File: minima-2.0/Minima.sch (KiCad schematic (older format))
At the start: 11 parts

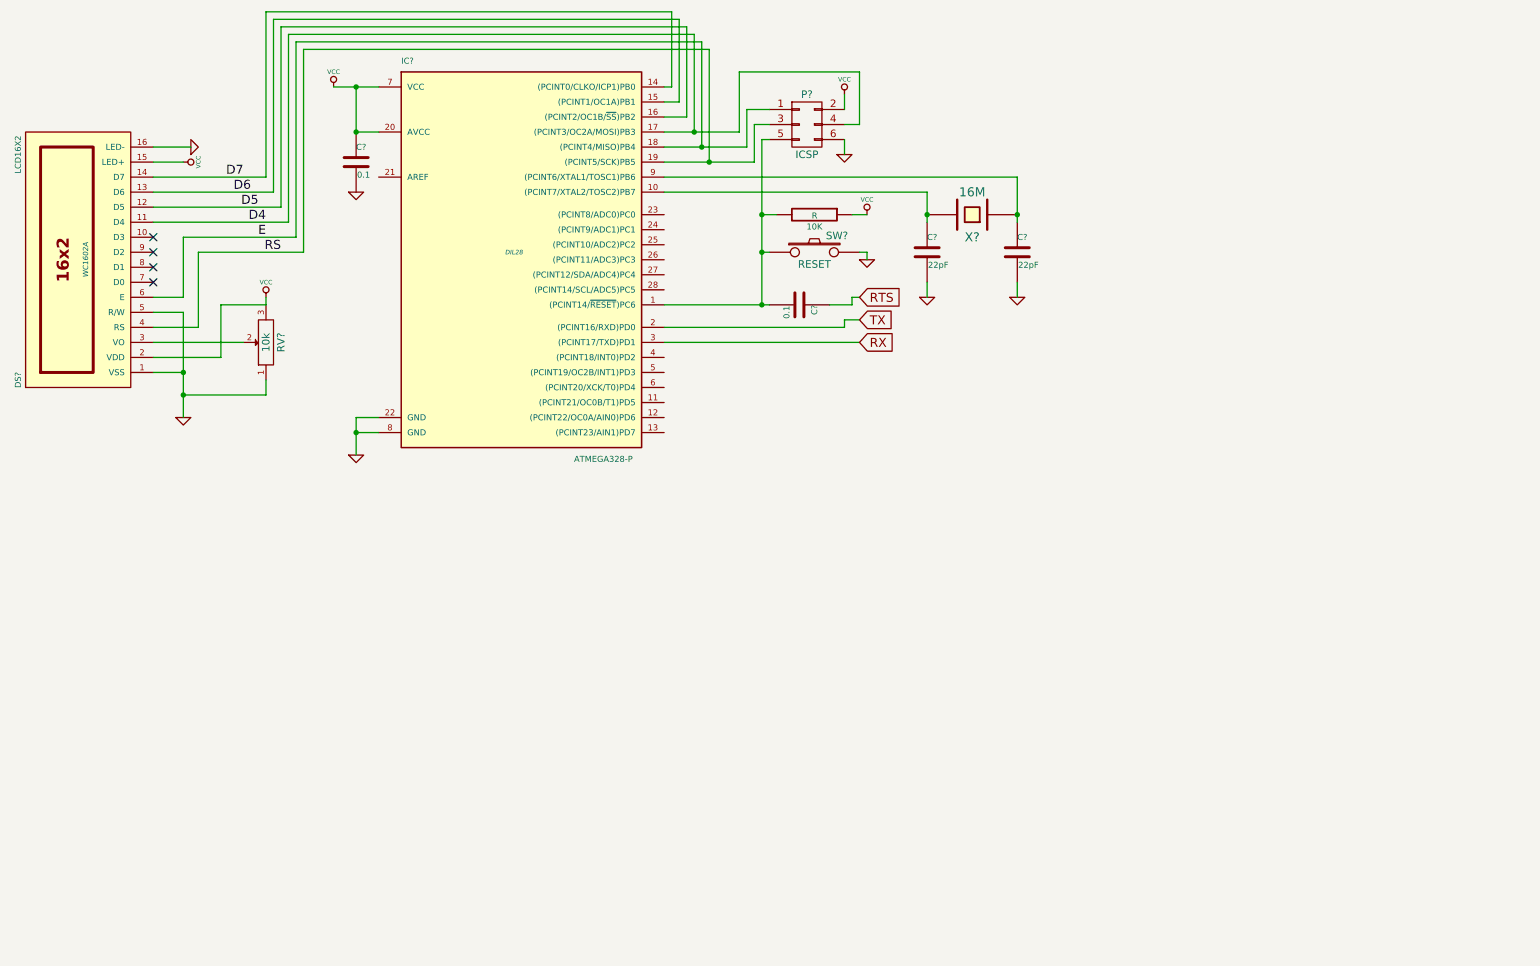
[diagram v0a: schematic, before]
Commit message: Finalized a first version of the front panel board
 - Added the Si570 on the front panel board
 - Split TX/RX and PTT
 - Inverted PD3 and PD4 for potential tone generator
 - Added multiple buttons via analog multiplexing
 - Added rotary encoder
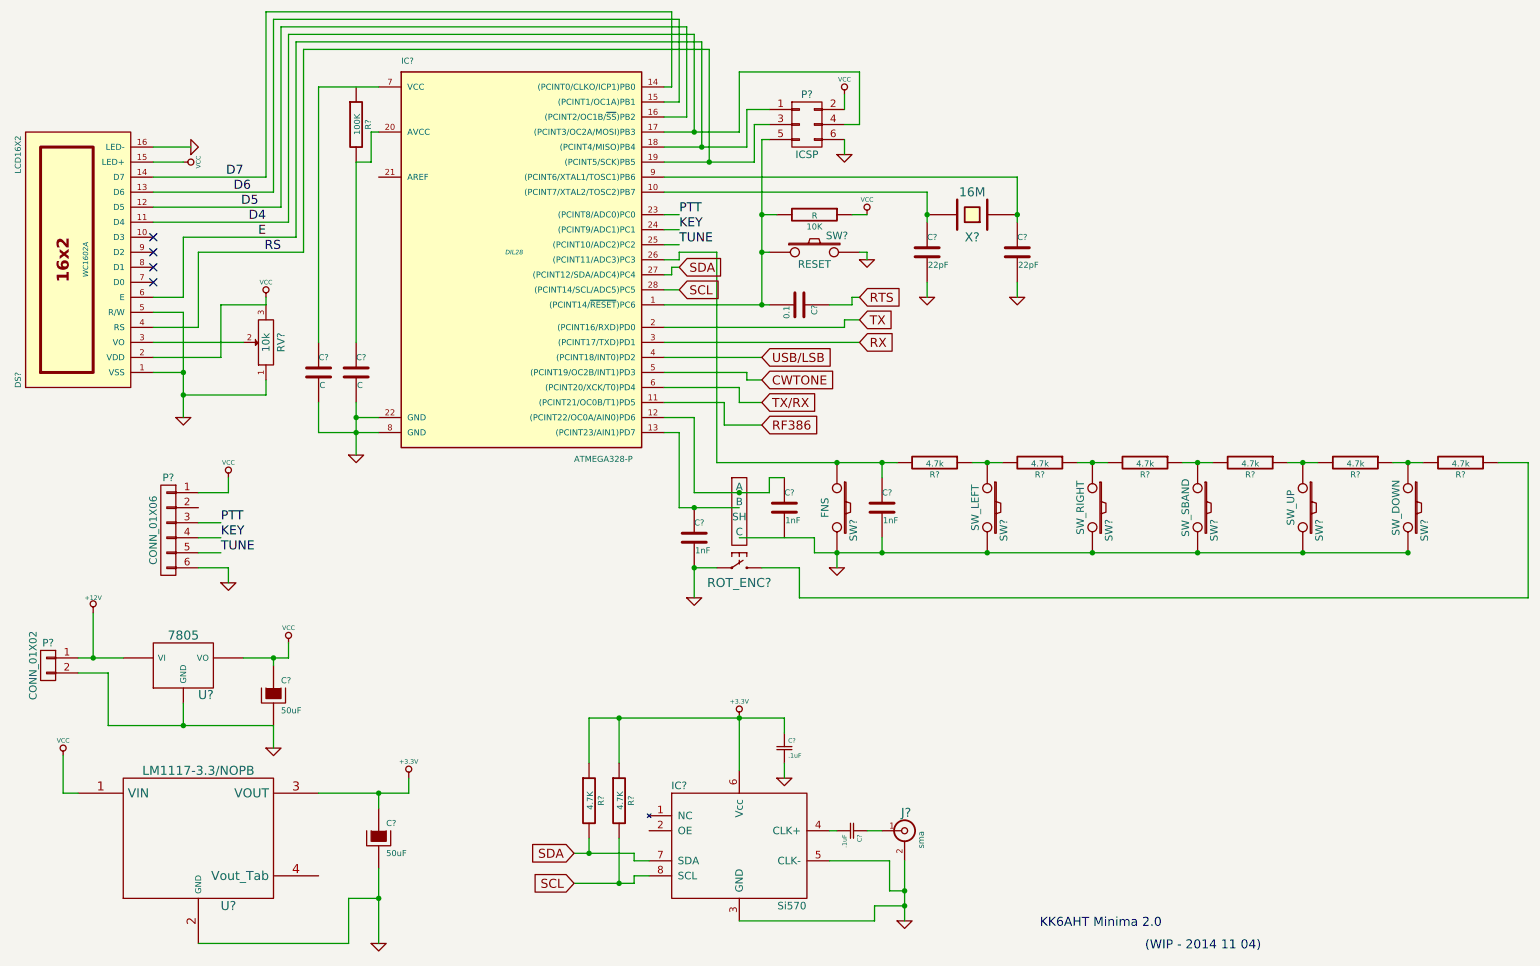
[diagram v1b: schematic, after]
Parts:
- removed C?: 0.1, symbol C
- added C? (x3): 1nF, symbol C
- added C? (x2): 50uF, symbol CP
- added C? (x2): .1uF, symbol Csmall
- added C? (x2): C, symbol C
- added IC?: Si570, SI570_SI571_Standard, symbol Si570
- added J?: sma, sma, symbol sma
- added P?: CONN_01X06, symbol CONN_01X06
- added P?: CONN_01X02, symbol CONN_01X02
- added R? (x6): 4.7k, symbol R
- added R? (x2): 4.7K, symbol R
- added R?: 100K, symbol R
- added ROT_ENC?: AB2_ROTARY_ENCODER_W_SW, symbol AB2_ROTARY_ENCODER_W_SW
- added SW?: FNS, symbol SW_PUSH
- added SW?: SW_LEFT, symbol SW_PUSH
- added SW?: SW_RIGHT, symbol SW_PUSH
- added SW?: SW_SBAND, symbol SW_PUSH
- added SW?: SW_UP, symbol SW_PUSH
- added SW?: SW_DOWN, symbol SW_PUSH
- added U?: LM1117-3.3/NOPB, SOT223, symbol LM1117-3.3/NOPB
- added U?: 7805, symbol 7805
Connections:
- net GND: now also C?.2, C?.2, C?.2, C?.2, C?.2, C?.2, C?.2, IC?.3 (GND), IC?.5 (CLK-), J?.2 (Ext), P?.2 (P2), P?.6 (P6), ROT_ENC?.2 (C), ROT_ENC?.4, SW?.2, SW?.2, SW?.2, SW?.2, SW?.2, SW?.2, U?.2 (GND), U?.GND
- net VCC: now also C?.1, P?.1 (P1), U?.1 (VIN), U?.VO; no longer IC?.20 (AVCC), IC?.7 (VCC)
- net RF386: now reaches IC?.11 ((PCINT21/OC0B/T1)PD5)
- net at IC?.12 ((PCINT22/OC0A/AIN0)PD6): now also C?.1, ROT_ENC?.1 (A)
- net at IC?.13 ((PCINT23/AIN1)PD7): now also C?.1, ROT_ENC?.3 (B)
- net PTT: now reaches IC?.23 ((PCINT8/ADC0)PC0)
- net PTT: now also P?.3 (P3)
- net KEY: now reaches IC?.24 ((PCINT9/ADC1)PC1)
- net KEY: now also P?.4 (P4)
- net TUNE: now reaches IC?.25 ((PCINT10/ADC2)PC2)
- net TUNE: now also P?.5 (P5)
- net at IC?.26 ((PCINT11/ADC3)PC3): now also C?.1, R?.2, SW?.1
- net SDA: now reaches IC?.27 ((PCINT12/SDA/ADC4)PC4)
- net SDA: now also IC?.7 (SDA), R?.2
- net SCL: now reaches IC?.28 ((PCINT14/SCL/ADC5)PC5)
- net SCL: now also IC?.8 (SCL), R?.2
- net USB/LSB: now reaches IC?.4 ((PCINT18/INT0)PD2)
- net CWTONE: now reaches IC?.5 ((PCINT19/OC2B/INT1)PD3)
- net TX/RX: now reaches IC?.6 ((PCINT20/XCK/T0)PD4)
- new net: C?.1, IC?.20 (AVCC), R?.2
- new net: C?.1, IC?.7 (VCC)
- new net: R?.1, ROT_ENC?.6
- new net: R?.1, R?.2, SW?.1 (x5)
- new net: C?.2, IC?.4 (CLK+)
- new net: C?.1, J?.1 (In)
- new net +12V: P?.1 (P1), U?.VI
- new net +3.3V: C?.1, C?.1, IC?.6 (Vcc), R?.1, R?.1, U?.3 (VOUT)
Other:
- note added: "(WIP - 2014 11 04)"
- note added: "KK6AHT Minima 2.0"
